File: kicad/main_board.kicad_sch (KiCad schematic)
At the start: 66 parts, among them J1 Conn_01x18, J2 Conn_01x18, J3 Conn_01x07, J4 Conn_01x07, J5 Conn_01x07, J6 Conn_01x07, J7 Conn_01x07, J8 TYPE-C-31-M-12, J9 TYPE-C-31-M-12, Q1 DMG2301L-7, Q2 DMG2301L-7, Q3 DMG2301L-7, Q4 DMG2301L-7, Q5 DMG2301L-7, SW1 Reset, SW2 Boot, U1 XC6220B331MR, U2 RP2040, U3 W25Q128JVS, U4 COS724, U5 COS724, U6 USBLC6-2SC6, U7 USBLC6-2SC6, Y1 Crystal_GND24

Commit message: Add production files for the PCBs
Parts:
- J1, J2, J3, J4, J5, J6, J7: now left out of the parts list
- R10, R11, R12, R13, R9: footprint Resistor_SMD:R_0402_1005Metric -> Resistor_SMD:R_0402_1005Metric_Pad0.72x0.64mm_HandSolder; JLCPCB P/N (none) -> C4109
- U3: JLCPCB P/N (none) -> C97521
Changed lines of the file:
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@@
       (effects (font (size 1.27 1.27)))
     )
-    (property "Footprint" "Resistor_SMD:R_0402_1005Metric" (at 255.27 90.17 0)
+    (property "Footprint" "Resistor_SMD:R_0402_1005Metric_Pad0.72x0.64mm_HandSolder" (at 255.27 90.17 0)
       (effects (font (size 1.27 1.27)) hide)
     )
     (property "Datasheet" "~" (at 255.27 90.17 0)
+      (effects (font (size 1.27 1.27)) hide)
+    )
+    (property "JLCPCB P/N" "C4109" (at 255.27 90.17 90)
       (effects (font (size 1.27 1.27)) hide)
     )
@@
       (effects (font (size 1.27 1.27)))
     )
-    (property "Footprint" "Resistor_SMD:R_0402_1005Metric" (at 255.27 116.84 0)
+    (property "Footprint" "Resistor_SMD:R_0402_1005Metric_Pad0.72x0.64mm_HandSolder" (at 255.27 116.84 0)
       (effects (font (size 1.27 1.27)) hide)
     )
     (property "Datasheet" "~" (at 255.27 116.84 0)
+      (effects (font (size 1.27 1.27)) hide)
+    )
+    (property "JLCPCB P/N" "C4109" (at 255.27 116.84 90)
       (effects (font (size 1.27 1.27)) hide)
     )
@@
       (effects (font (size 1.27 1.27)))
     )
-    (property "Footprint" "Resistor_SMD:R_0402_1005Metric" (at 255.27 143.51 0)
+    (property "Footprint" "Resistor_SMD:R_0402_1005Metric_Pad0.72x0.64mm_HandSolder" (at 255.27 143.51 0)
       (effects (font (size 1.27 1.27)) hide)
     )
     (property "Datasheet" "~" (at 255.27 143.51 0)
+      (effects (font (size 1.27 1.27)) hide)
+    )
+    (property "JLCPCB P/N" "C4109" (at 255.27 143.51 90)
       (effects (font (size 1.27 1.27)) hide)
     )
@@
       (effects (font (size 1.27 1.27)))
     )
-    (property "Footprint" "Resistor_SMD:R_0402_1005Metric" (at 255.27 172.72 0)
+    (property "Footprint" "Resistor_SMD:R_0402_1005Metric_Pad0.72x0.64mm_HandSolder" (at 255.27 172.72 0)
       (effects (font (size 1.27 1.27)) hide)
     )
     (property "Datasheet" "~" (at 255.27 172.72 0)
+      (effects (font (size 1.27 1.27)) hide)
+    )
+    (property "JLCPCB P/N" "C4109" (at 255.27 172.72 90)
       (effects (font (size 1.27 1.27)) hide)
     )
@@
       (effects (font (size 1.27 1.27)) hide)
     )
+    (property "JLCPCB P/N" "C97521" (at 162.56 271.78 0)
+      (effects (font (size 1.27 1.27)) hide)
+    )
     (pin "1")
     (pin "2")
@@
   )
   (symbol (lib_id "Connector_Generic:Conn_01x07") (at 326.39 85.09 0) (mirror x) (unit 1)
-    (in_bom yes) (on_board yes) (dnp no)
+    (in_bom no) (on_board yes) (dnp no)
     (property "Reference" "J4" (at 328.422 86.1568 0)
       (effects (font (size 1.27 1.27)) (justify left))
@@
   )
   (symbol (lib_id "Connector_Generic:Conn_01x07") (at 326.39 116.84 0) (mirror x) (unit 1)
-    (in_bom yes) (on_board yes) (dnp no)
+    (in_bom no) (on_board yes) (dnp no)
     (property "Reference" "J5" (at 328.422 117.9068 0)
       (effects (font (size 1.27 1.27)) (justify left))
@@
   )
   (symbol (lib_id "Connector_Generic:Conn_01x18") (at 76.2 347.98 0) (unit 1)
-    (in_bom yes) (on_board yes) (dnp no) (fields_autoplaced)
+    (in_bom no) (on_board yes) (dnp no) (fields_autoplaced)
     (property "Reference" "J2" (at 78.232 348.4153 0)
       (effects (font (size 1.27 1.27)) (justify left))
@@
   )
   (symbol (lib_id "Connector_Generic:Conn_01x07") (at 326.39 148.59 0) (mirror x) (unit 1)
-    (in_bom yes) (on_board yes) (dnp no)
+    (in_bom no) (on_board yes) (dnp no)
     (property "Reference" "J6" (at 328.422 149.6568 0)
       (effects (font (size 1.27 1.27)) (justify left))
@@
   )
   (symbol (lib_id "Connector_Generic:Conn_01x18") (at 43.18 347.98 0) (unit 1)
-    (in_bom yes) (on_board yes) (dnp no) (fields_autoplaced)
+    (in_bom no) (on_board yes) (dnp no) (fields_autoplaced)
     (property "Reference" "J1" (at 45.212 348.4153 0)
       (effects (font (size 1.27 1.27)) (justify left))
@@
   )
   (symbol (lib_id "Connector_Generic:Conn_01x07") (at 326.39 180.34 0) (mirror x) (unit 1)
-    (in_bom yes) (on_board yes) (dnp no)
+    (in_bom no) (on_board yes) (dnp no)
     (property "Reference" "J7" (at 328.422 181.4068 0)
       (effects (font (size 1.27 1.27)) (justify left))
@@
       (effects (font (size 1.27 1.27)))
     )
-    (property "Footprint" "Resistor_SMD:R_0402_1005Metric" (at 255.27 199.39 0)
+    (property "Footprint" "Resistor_SMD:R_0402_1005Metric_Pad0.72x0.64mm_HandSolder" (at 255.27 199.39 0)
       (effects (font (size 1.27 1.27)) hide)
     )
     (property "Datasheet" "~" (at 255.27 199.39 0)
+      (effects (font (size 1.27 1.27)) hide)
+    )
+    (property "JLCPCB P/N" "C4109" (at 255.27 199.39 90)
       (effects (font (size 1.27 1.27)) hide)
     )
@@
   )
   (symbol (lib_id "Connector_Generic:Conn_01x07") (at 326.39 53.34 0) (mirror x) (unit 1)
-    (in_bom yes) (on_board yes) (dnp no)
+    (in_bom no) (on_board yes) (dnp no)
     (property "Reference" "J3" (at 328.422 54.4068 0)
       (effects (font (size 1.27 1.27)) (justify left))

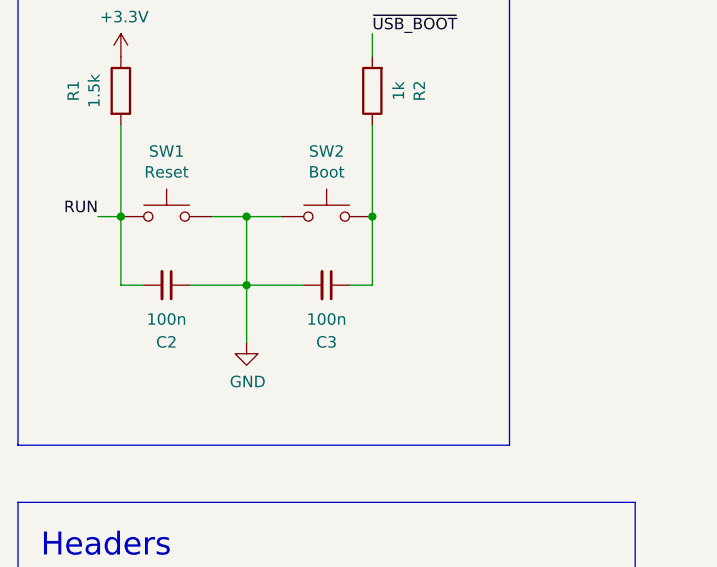
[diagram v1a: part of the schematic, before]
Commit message: Main board v2.5.1
- Remove the decoupling capacitor on the boot selection button
- Fix the part selection in the BOM for the 27 ohm usb series resistors
(old part was mistakenly a 27kohm resistor)
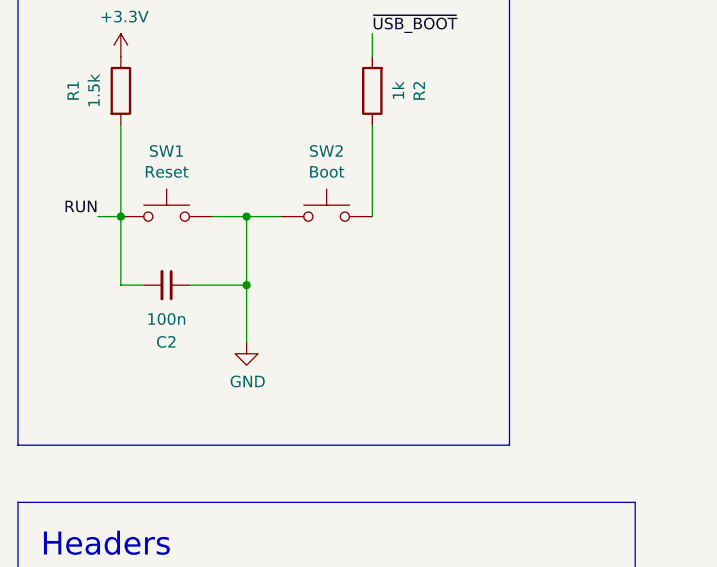
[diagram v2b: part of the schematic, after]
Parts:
- removed C3: 100n, Capacitor_SMD:C_0402_1005Metric, symbol Device:C_Small
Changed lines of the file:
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@@
   (junction (at 124.46 57.15) (diameter 0) (color 0 0 0 0)
-  )
-  (junction (at 64.77 280.67) (diameter 0) (color 0 0 0 0)
   )
   (junction (at 104.14 57.15) (diameter 0) (color 0 0 0 0)
@@
     (stroke (width 0) (type default))
   )
-  (wire (pts (xy 57.15 288.29) (xy 50.8 288.29))
-    (stroke (width 0) (type default))
-  )
   (wire (pts (xy 76.2 104.14) (xy 62.23 104.14))
     (stroke (width 0) (type default))
@@
     (stroke (width 0) (type default))
   )
-  (wire (pts (xy 64.77 288.29) (xy 62.23 288.29))
-    (stroke (width 0) (type default))
-  )
   (wire (pts (xy 370.84 80.01) (xy 370.84 82.55))
     (stroke (width 0) (type default))
@@
   )
   (wire (pts (xy 62.23 97.79) (xy 76.2 97.79))
-    (stroke (width 0) (type default))
-  )
-  (wire (pts (xy 64.77 280.67) (xy 64.77 288.29))
     (stroke (width 0) (type default))
   )
@@
         )
       )
-    )
-  )
-  (symbol (lib_id "Device:C_Small") (at 59.69 288.29 270) (unit 1)
-    (in_bom yes) (on_board yes) (dnp no)
-    (property "Reference" "C3" (at 59.69 294.64 90)
-      (effects (font (size 1.27 1.27)))
-    )
-    (property "Value" "100n" (at 59.69 292.1 90)
-      (effects (font (size 1.27 1.27)))
-    )
-    (property "Footprint" "Capacitor_SMD:C_0402_1005Metric" (at 59.69 288.29 0)
-      (effects (font (size 1.27 1.27)) hide)
-    )
-    (property "Datasheet" "~" (at 59.69 288.29 0)
-      (effects (font (size 1.27 1.27)) hide)
-    )
-    (property "JLCPCB P/N" "C307331" (at 59.69 288.29 90)
-      (effects (font (size 1.27 1.27)) hide)
-    )
-    (pin "1")
-    (pin "2")
-    (instances
-      (project "main_board"
-        (path "/3c082c72-c82b-4256-b7a7-9c550c226441"
-          (reference "C3") (unit 1)
-        )
-      )

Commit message: Added correct LCSC part number for USB termination resistor
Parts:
- R5, R6: JLCPCB P/N C25771 -> C25100
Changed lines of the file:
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@@
       (effects (font (size 1.27 1.27)) hide)
     )
-    (property "JLCPCB P/N" "C25771" (at 154.94 72.39 90)
+    (property "JLCPCB P/N" "C25100" (at 154.94 72.39 90)
       (effects (font (size 1.27 1.27)) hide)
     )
@@
       (effects (font (size 1.27 1.27)) hide)
     )
-    (property "JLCPCB P/N" "C25771" (at 154.94 80.01 90)
-      (effects (font (size 1.27 1.27)) hide)
-    )
+    (property "JLCPCB P/N" "C25100" (at 154.94 80.01 90)
+      (effects (font (size 1.27 1.27)) hide)
+    )
